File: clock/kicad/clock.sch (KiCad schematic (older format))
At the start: 75 parts, among them J1 USB-SS-52100-001, Q1 PN2222A, SW1 HOUR, SW2 MIN, SW3 TIME, U1 74HC4060, U10 74HC390, U11 NE555P, U12 74HC4511, U13 74HC4511, U14 74HC4511, U15 74HC4511, U16 74HC4511, U17 74HC4511, U18 KCSC02-105, U19 KCSC02-105, U2 LM317L_TO92, U20 KCSC02-105, U21 KCSC02-105, U22 KCSC02-105, U23 KCSC02-105, U3 74HC14, U4 74HC157, U5 SN74HC74N, U6 74HC390, U7 74HC08, U8 74HC390, U9 74HC08

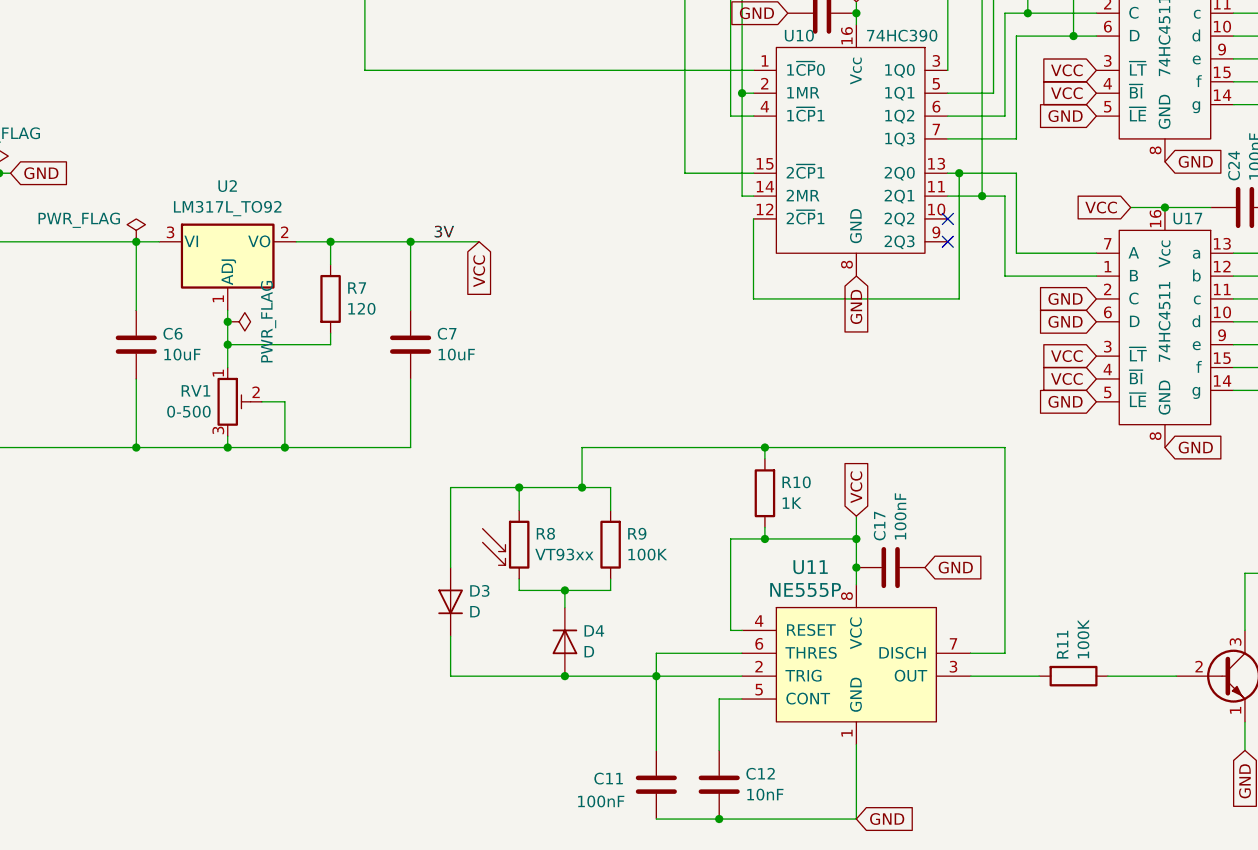
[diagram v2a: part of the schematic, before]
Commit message: Clock: Tweak PWM RC values.
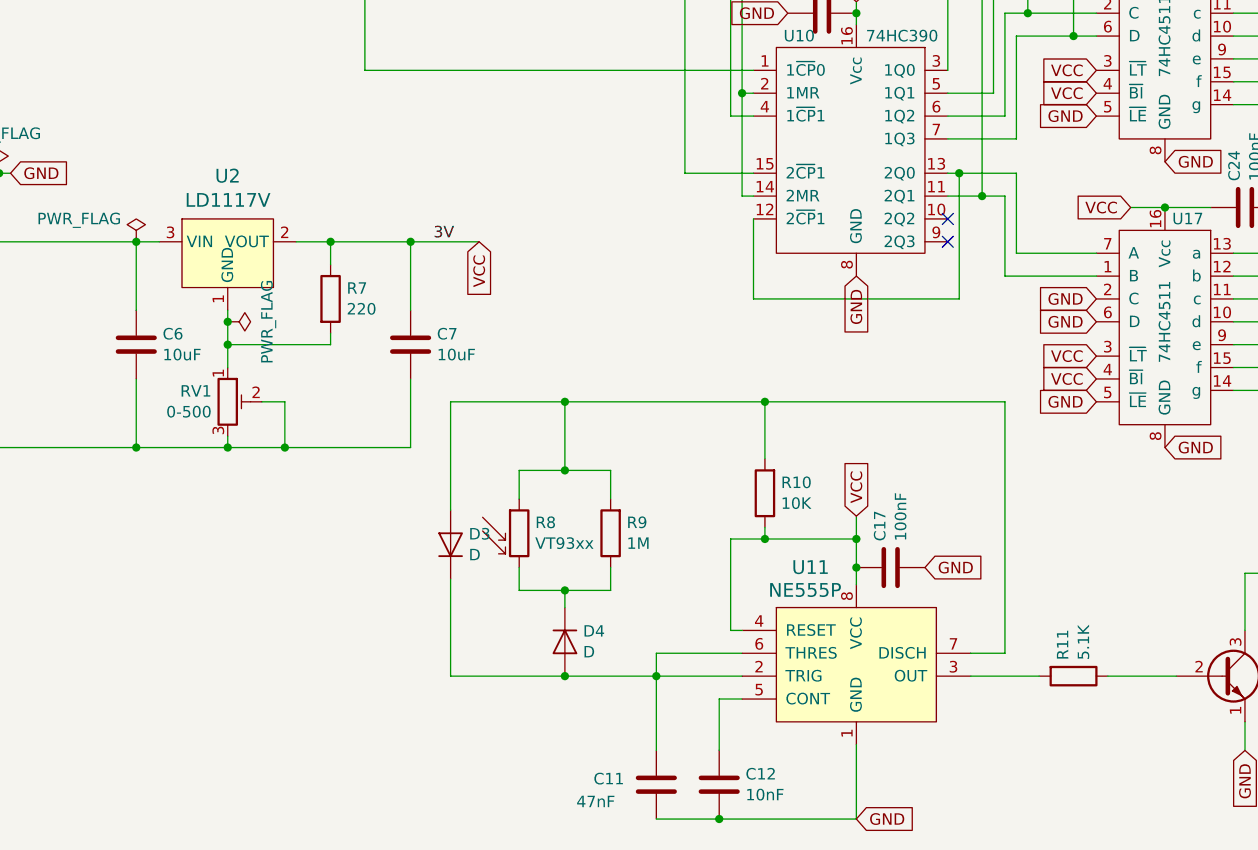
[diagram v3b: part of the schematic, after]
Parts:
- removed U2: LM317L_TO92, Package_TO_SOT_THT:TO-92_Inline_Wide, symbol Regulator_Linear:LM317L_TO92
- added U2: LD1117V, digikey-footprints:TO-220-3, symbol clock:LD1117V
- C11: value 100nF -> 47nF
- C7: footprint Capacitor_THT:C_Disc_D5.0mm_W2.5mm_P2.50mm -> Capacitor_THT:C_Radial_D5.0mm_H11.0mm_P2.00mm
- R10: value 1K -> 10K
- R11: value 100K -> 5.1K
- R7: value 120 -> 220
- R9: value 100K -> 1M
- U5: footprint Package_DIP:DIP-14_W7.62mm_Socket -> clock:Socket_DIP-14_0.775in_Conn
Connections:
- net 5V: now also U2.3 (VIN)
- net VCC: now also U2.2 (VOUT)
- net at R7.2, RV1.1: now also U2.1 (GND)
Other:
- moved on the sheet: D3, R8, R9
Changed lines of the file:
@@
 F 0 "U5" H 3750 2200 60  0000 C CNN
 F 1 "SN74HC74N" H 3800 2350 60  0000 C CNN
-F 2 "Package_DIP:DIP-14_W7.62mm_Socket" H 4200 1950 60  0001 L CNN
+F 2 "clock:Socket_DIP-14_0.775in_Conn" H 4200 1950 60  0001 L CNN
 F 3 "http://www.ti.com/general/docs/suppproductinfo.tsp?distId=10&gotoUrl=http%3A%2F%2Fwww.ti.com%2Flit%2Fgpn%2Fsn74hc74" H 4200 2050 60  0001 L CNN
 F 4 "296-1602-5-ND" H 4200 2150 60  0001 L CNN "Digi-Key_PN"
@@
 P 4875 11825
 F 0 "C11" H 4600 11850 50  0000 L CNN
-F 1 "100nF" H 4525 11750 50  0000 L CNN
+F 1 "47nF" H 4525 11750 50  0000 L CNN
 F 2 "Capacitor_THT:C_Disc_D5.0mm_W2.5mm_P2.50mm" H 4913 11675 50  0001 C CNN
 F 3 "~" H 4875 11825 50  0001 C CNN
@@
 L Device:D D3
 U 1 1 5DB771DB
-P 3975 11025
-F 0 "D3" V 4021 10946 50  0000 R CNN
-F 1 "D" V 3930 10946 50  0000 R CNN
-F 2 "digikey-footprints:Diode_DO-35_P10mm" H 3975 11025 50  0001 C CNN
-F 3 "~" H 3975 11025 50  0001 C CNN
-	1    3975 11025
+P 3975 10775
+F 0 "D3" V 4021 10696 50  0000 R CNN
+F 1 "D" V 3930 10696 50  0000 R CNN
+F 2 "digikey-footprints:Diode_DO-35_P10mm" H 3975 10775 50  0001 C CNN
+F 3 "~" H 3975 10775 50  0001 C CNN
+	1    3975 10775
 	0    -1   -1   0
 $EndComp
@@
 L Device:R R9
 U 1 1 5DB7BBEA
-P 4675 10775
-F 0 "R9" H 4605 10729 50  0000 R CNN
-F 1 "100K" H 4605 10820 50  0000 R CNN
-F 2 "Resistor_THT:R_Axial_DIN0207_L6.3mm_D2.5mm_P7.62mm_Horizontal" V 4605 10775 50  0001 C CNN
-F 3 "~" H 4675 10775 50  0001 C CNN
-	1    4675 10775
+P 4675 10725
+F 0 "R9" H 4605 10679 50  0000 R CNN
+F 1 "1M" H 4605 10770 50  0000 R CNN
+F 2 "Resistor_THT:R_Axial_DIN0207_L6.3mm_D2.5mm_P7.62mm_Horizontal" V 4605 10725 50  0001 C CNN
+F 3 "~" H 4675 10725 50  0001 C CNN
+	1    4675 10725
 	-1   0    0    1
 $EndComp
@@
 	3975 11350 4475 11350
 Wire Wire Line
-	4675 10525 4675 10625
-Wire Wire Line
 	6250 11250 6400 11250
 Wire Wire Line
-	6400 11250 6400 10350
-Wire Wire Line
-	6400 10350 5350 10350
-Connection ~ 4550 10525
-Wire Wire Line
-	4550 10525 4675 10525
-Wire Wire Line
-	3975 10525 4275 10525
+	6400 11250 6400 10150
+Wire Wire Line
+	6400 10150 5350 10150
 $Comp
 L Sensor_Optical:VT93xx R8
 U 1 1 5DC80BDF
-P 4275 10775
-F 0 "R8" H 4345 10821 50  0000 L CNN
-F 1 "VT93xx" H 4345 10730 50  0000 L CNN
-F 2 "OptoDevice:R_LDR_4.9x4.2mm_P2.54mm_Vertical" V 4450 10775 50  0001 C CNN
-F 3 "http://www.produktinfo.conrad.com/datenblaetter/125000-149999/140375-da-01-en-FOTOWIDERSTAND__VT_93_N2__THT_.pdf" H 4275 10725 50  0001 C CNN
-	1    4275 10775
+P 4275 10725
+F 0 "R8" H 4345 10771 50  0000 L CNN
+F 1 "VT93xx" H 4345 10680 50  0000 L CNN
+F 2 "OptoDevice:R_LDR_4.9x4.2mm_P2.54mm_Vertical" V 4450 10725 50  0001 C CNN
+F 3 "http://www.produktinfo.conrad.com/datenblaetter/125000-149999/140375-da-01-en-FOTOWIDERSTAND__VT_93_N2__THT_.pdf" H 4275 10675 50  0001 C CNN
+	1    4275 10725
 	1    0    0    -1
 $EndComp
@@
 	4475 11350 4875 11350
 Wire Wire Line
-	4550 10350 4550 10525
-Wire Wire Line
-	4275 10925 4275 10975
-Wire Wire Line
 	4275 10975 4475 10975
 Wire Wire Line
-	4675 10975 4675 10925
+	4675 10975 4675 10875
 Wire Wire Line
 	4475 11050 4475 10975
@@
 	4475 10975 4675 10975
 Wire Wire Line
-	4275 10625 4275 10525
-Connection ~ 4275 10525
-Wire Wire Line
-	4275 10525 4550 10525
-Wire Wire Line
-	3975 11175 3975 11350
-Wire Wire Line
-	3975 10875 3975 10525
+	3975 10925 3975 11350
+Wire Wire Line
+	3975 10625 3975 10150
 $Comp
 L Transistor_BJT:PN2222A Q1
@@
 P 6700 11350
 F 0 "R11" H 6630 11304 50  0000 R CNN
-F 1 "100K" H 6630 11395 50  0000 R CNN
+F 1 "5.1K" H 6630 11395 50  0000 R CNN
 F 2 "Resistor_THT:R_Axial_DIN0207_L6.3mm_D2.5mm_P7.62mm_Horizontal" V 6630 11350 50  0001 C CNN
 F 3 "~" H 6700 11350 50  0001 C CNN
@@
 P 5350 10550
 F 0 "R10" H 5280 10504 50  0000 R CNN
-F 1 "1K" H 5280 10595 50  0000 R CNN
+F 1 "10K" H 5280 10595 50  0000 R CNN
 F 2 "Resistor_THT:R_Axial_DIN0207_L6.3mm_D2.5mm_P7.62mm_Horizontal" V 5280 10550 50  0001 C CNN
 F 3 "~" H 5350 10550 50  0001 C CNN
@@
 	5350 10750 5750 10750
 Wire Wire Line
-	5350 10400 5350 10350
-Connection ~ 5350 10350
-Wire Wire Line
-	5350 10350 4550 10350
+	5350 10400 5350 10150
 Connection ~ 2550 1050
 Wire Wire Line
@@
 P 3450 9700
 F 0 "R7" H 3520 9746 50  0000 L CNN
-F 1 "120" H 3520 9655 50  0000 L CNN
+F 1 "220" H 3520 9655 50  0000 L CNN
 F 2 "Resistor_THT:R_Axial_DIN0207_L6.3mm_D2.5mm_P7.62mm_Horizontal" V 3380 9700 50  0001 C CNN
 F 3 "~" H 3450 9700 50  0001 C CNN
@@
 F 0 "C7" H 3915 9946 50  0000 L CNN
 F 1 "10uF" H 3915 9855 50  0000 L CNN
-F 2 "Capacitor_THT:C_Disc_D5.0mm_W2.5mm_P2.50mm" H 3838 9750 50  0001 C CNN
+F 2 "Capacitor_THT:C_Radial_D5.0mm_H11.0mm_P2.00mm" H 3838 9750 50  0001 C CNN
 F 3 "~" H 3800 9900 50  0001 C CNN
 	1    3800 9900
@@
 Wire Wire Line
 	9700 8750 9900 8750
-$Comp
-L Regulator_Linear:LM317L_TO92 U2
-U 1 1 60F323F5
-P 3000 9450
-F 0 "U2" H 3000 9692 50  0000 C CNN
-F 1 "LM317L_TO92" H 3000 9601 50  0000 C CNN
-F 2 "Package_TO_SOT_THT:TO-92_Inline_Wide" H 3000 9675 50  0001 C CIN
-F 3 "http://www.ti.com/lit/ds/snvs775k/snvs775k.pdf" H 3000 9450 50  0001 C CNN
-	1    3000 9450
-	1    0    0    -1
-$EndComp
 Wire Wire Line
 	7400 9900 9600 9900
@@
 Wire Wire Line
 	3250 10350 3000 10350
+$Comp
+L clock:LD1117V U2
+U 1 1 611BD3B2
+P 3000 9450
+F 0 "U2" H 3000 9737 60  0000 C CNN
+F 1 "LD1117V" H 3000 9631 60  0000 C CNN
+F 2 "digikey-footprints:TO-220-3" H 3200 9650 60  0001 L CNN
+F 3 "http://www.st.com/content/ccc/resource/technical/document/datasheet/99/3b/7d/91/91/51/4b/be/CD00000544.pdf/files/CD00000544.pdf/jcr:content/translations/en.CD00000544.pdf" H 3200 9750 60  0001 L CNN
+F 4 "497-7310-5-ND" H 3200 9850 60  0001 L CNN "Digi-Key_PN"
+F 5 "LD1117V" H 3200 9950 60  0001 L CNN "MPN"
+F 6 "Integrated Circuits (ICs)" H 3200 10050 60  0001 L CNN "Category"
+F 7 "PMIC - Voltage Regulators - Linear" H 3200 10150 60  0001 L CNN "Family"
+F 8 "http://www.st.com/content/ccc/resource/technical/document/datasheet/99/3b/7d/91/91/51/4b/be/CD00000544.pdf/files/CD00000544.pdf/jcr:content/translations/en.CD00000544.pdf" H 3200 10250 60  0001 L CNN "DK_Datasheet_Link"
+F 9 "/product-detail/en/stmicroelectronics/LD1117V33/497-1491-5-ND/586012" H 3200 10350 60  0001 L CNN "DK_Detail_Page"
+F 10 "IC REG LINEAR 1.8V-5V 800MA TO220AB" H 3200 10450 60  0001 L CNN "Description"
+F 11 "STMicroelectronics" H 3200 10550 60  0001 L CNN "Manufacturer"
+F 12 "Active" H 3200 10650 60  0001 L CNN "Status"
+	1    3000 9450
+	1    0    0    -1
+$EndComp
+Connection ~ 5350 10150
+Wire Wire Line
+	4275 10875 4275 10975
+Wire Wire Line
+	3975 10150 4475 10150
+Wire Wire Line
+	4275 10575 4275 10450
+Wire Wire Line
+	4275 10450 4475 10450
+Wire Wire Line
+	4675 10450 4675 10575
+Wire Wire Line
+	4475 10450 4475 10150
+Connection ~ 4475 10450
+Wire Wire Line
+	4475 10450 4675 10450
+Connection ~ 4475 10150
+Wire Wire Line
+	4475 10150 5350 10150
 $EndSCHEMATC

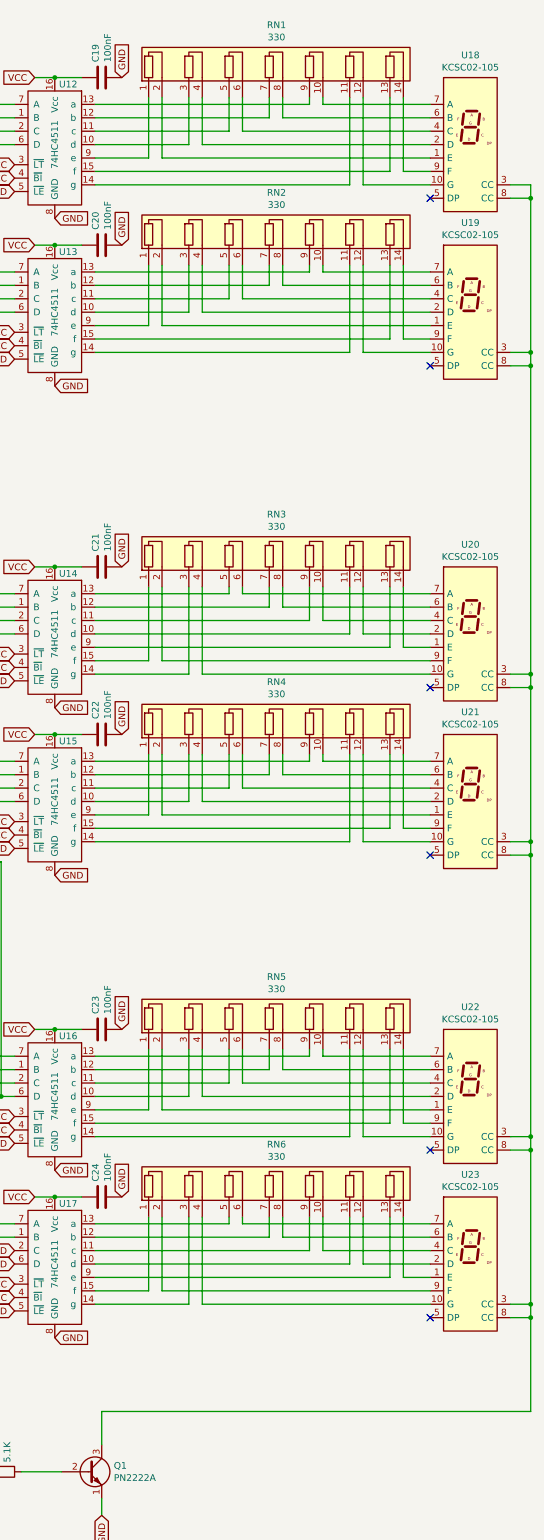
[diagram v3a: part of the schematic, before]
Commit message: Clock: Changed Resistor Networks to real parts.
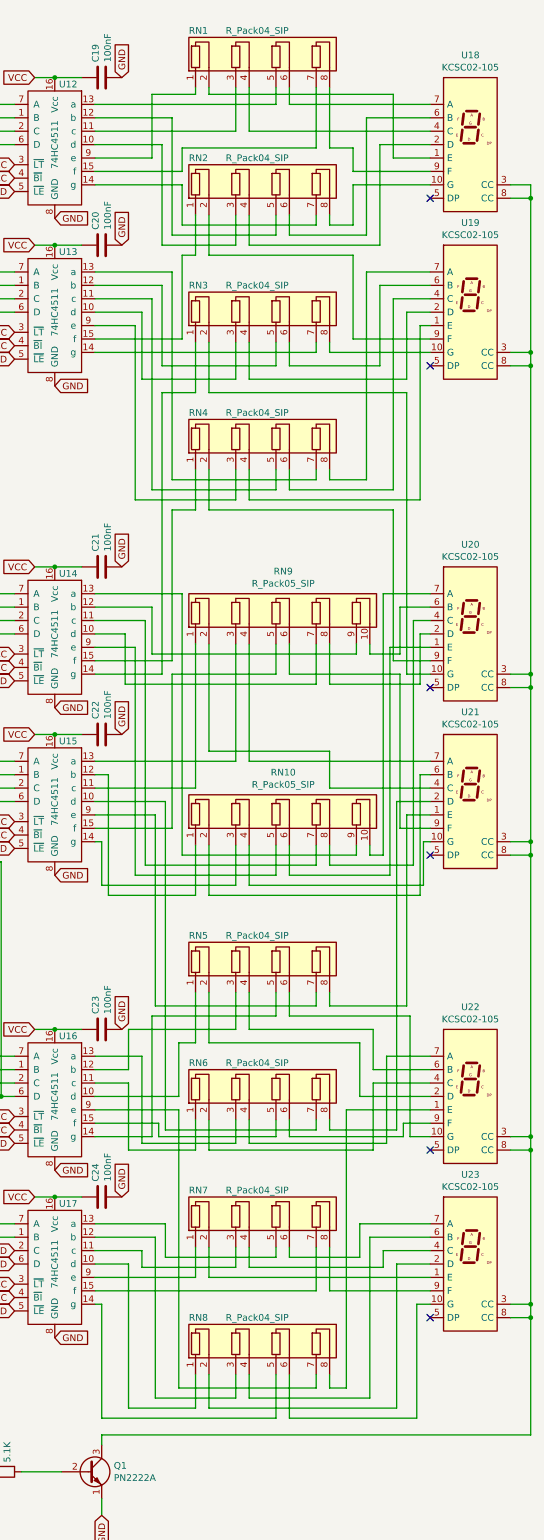
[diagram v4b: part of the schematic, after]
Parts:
- removed RN1, RN2, RN3, RN4, RN5, RN6: 330, Resistor_THT:R_Array_SIP14, symbol Device:R_Pack07_SIP
- added RN1, RN2, RN3, RN4, RN5, RN6, RN7, RN8: R_Pack04_SIP, Resistor_THT:R_Array_SIP8, symbol Device:R_Pack04_SIP
- added RN10, RN9: R_Pack05_SIP, Resistor_THT:R_Array_SIP10, symbol Device:R_Pack05_SIP
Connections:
- net at U12.10 (d): now also RN2.3 (R2.1)
- net at U12.11 (c): now also RN1.3 (R2.1)
- net at U12.12 (b): now also RN2.5 (R3.1)
- net at U12.13 (a): now also RN1.5 (R3.1)
- net at U12.14 (g): now also RN2.7 (R4.1)
- net at U12.15 (f): now also RN1.7 (R4.1)
- net at U12.9 (e): now also RN1.1 (R1.1)
- net at U13.10 (d): now also RN3.3 (R2.1)
- net at U13.11 (c): now also RN4.5 (R3.1)
- net at U13.12 (b): now also RN3.5 (R3.1)
- net at U13.13 (a): now also RN4.7 (R4.1)
- net at U13.14 (g): now also RN3.7 (R4.1)
- net at U13.15 (f): now also RN2.1 (R1.1)
- net at U13.9 (e): now also RN4.3 (R2.1)
- net at U18.1 (E): now also RN1.2 (R1.2)
- net at U18.10 (G): now also RN2.8 (R4.2)
- net at U18.2 (D): now also RN2.4 (R2.2)
- net at U18.4 (C): now also RN1.4 (R2.2)
- net at U18.6 (B): now also RN2.6 (R3.2)
- net at U18.7 (A): now also RN1.6 (R3.2)
- net at U18.9 (F): now also RN1.8 (R4.2)
- net at U19.1 (E): now also RN4.4 (R2.2)
- net at U19.10 (G): now also RN3.8 (R4.2)
- net at U19.2 (D): now also RN3.4 (R2.2)
- net at U19.4 (C): now also RN4.6 (R3.2)
- net at U19.6 (B): now also RN3.6 (R3.2)
- net at U19.7 (A): now also RN4.8 (R4.2)
- net at U19.9 (F): now also RN2.2 (R1.2)
- net at U14.10 (d): now also RN9.7 (R4.1)
- net at U14.11 (c): now also RN10.7 (R4.1)
- net at U14.12 (b): now also RN9.9 (R5.1)
- net at U14.13 (a): now also RN10.9 (R5.1)
- net at U14.14 (g): now also RN3.1 (R1.1)
- net at U14.15 (f): now also RN4.1 (R1.1)
- net at U14.9 (e): now also RN10.5 (R3.1)
- net at U15.10 (d): now also RN6.7 (R4.1)
- net at U15.11 (c): now also RN9.1 (R1.1)
- net at U15.12 (b): now also RN10.1 (R1.1)
- net at U15.13 (a): now also RN9.3 (R2.1)
- net at U15.14 (g): now also RN10.3 (R2.1)
- net at U15.15 (f): now also RN9.5 (R3.1)
- net at U15.9 (e): now also RN5.7 (R4.1)
- net at U20.1 (E): now also RN10.6 (R3.2)
- net at U20.10 (G): now also RN3.2 (R1.2)
- net at U20.2 (D): now also RN9.8 (R4.2)
- net at U20.4 (C): now also RN10.8 (R4.2)
- net at U20.6 (B): now also RN9.10 (R5.2)
- net at U20.7 (A): now also RN10.10 (R5.2)
- net at U20.9 (F): now also RN4.2 (R1.2)
- net at U21.1 (E): now also RN5.8 (R4.2)
- net at U21.10 (G): now also RN10.4 (R2.2)
- net at U21.2 (D): now also RN6.8 (R4.2)
- net at U21.4 (C): now also RN9.2 (R1.2)
- net at U21.6 (B): now also RN10.2 (R1.2)
- net at U21.7 (A): now also RN9.4 (R2.2)
- net at U21.9 (F): now also RN9.6 (R3.2)
- net at U16.10 (d): now also RN5.1 (R1.1)
- net at U16.11 (c): now also RN6.1 (R1.1)
- net at U16.12 (b): now also RN5.3 (R2.1)
- net at U16.13 (a): now also RN6.3 (R2.1)
- net at U16.14 (g): now also RN5.5 (R3.1)
- net at U16.15 (f): now also RN6.5 (R3.1)
- net at U16.9 (e): now also RN8.7 (R4.1)
- net at U17.10 (d): now also RN8.1 (R1.1)
- net at U17.11 (c): now also RN7.3 (R2.1)
- net at U17.12 (b): now also RN8.3 (R2.1)
- net at U17.13 (a): now also RN7.5 (R3.1)
- net at U17.14 (g): now also RN8.5 (R3.1)
- net at U17.15 (f): now also RN7.7 (R4.1)
- net at U17.9 (e): now also RN7.1 (R1.1)
- net at U22.1 (E): now also RN8.8 (R4.2)
- net at U22.10 (G): now also RN5.6 (R3.2)
- net at U22.2 (D): now also RN5.2 (R1.2)
- net at U22.4 (C): now also RN6.2 (R1.2)
- net at U22.6 (B): now also RN5.4 (R2.2)
- net at U22.7 (A): now also RN6.4 (R2.2)
- net at U22.9 (F): now also RN6.6 (R3.2)
- net at U23.1 (E): now also RN7.2 (R1.2)
- net at U23.10 (G): now also RN8.6 (R3.2)
- net at U23.2 (D): now also RN8.2 (R1.2)
- net at U23.4 (C): now also RN7.4 (R2.2)
- net at U23.6 (B): now also RN8.4 (R2.2)
- net at U23.7 (A): now also RN7.6 (R3.2)
- net at U23.9 (F): now also RN7.8 (R4.2)
